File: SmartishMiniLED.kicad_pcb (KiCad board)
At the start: 2 copper layers, 24.9 x 55.4 mm, 35 parts, among them J1 USB_C_Receptacle_USB2.0, J2 BUTTON, J3 Screw_Terminal_01x03, P1 NeopixelStripPads, P2 NeopixelStripPads, Q1 MMBT2222, Q2 MMBT2222, Q3 IRLML6344, Q4 IRF7410, SW2 TL3342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

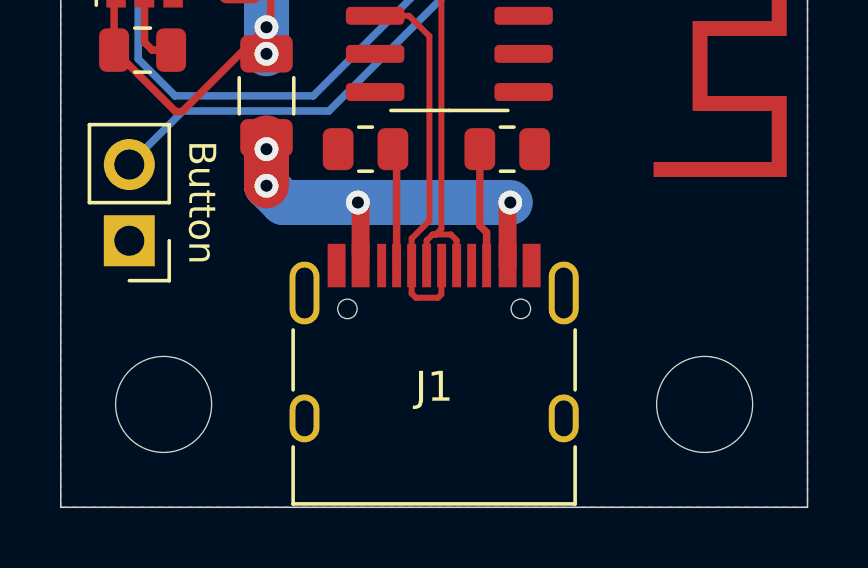
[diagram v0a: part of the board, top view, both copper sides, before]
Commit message: Added some pads on the back for as an alternative to supplying the main power.
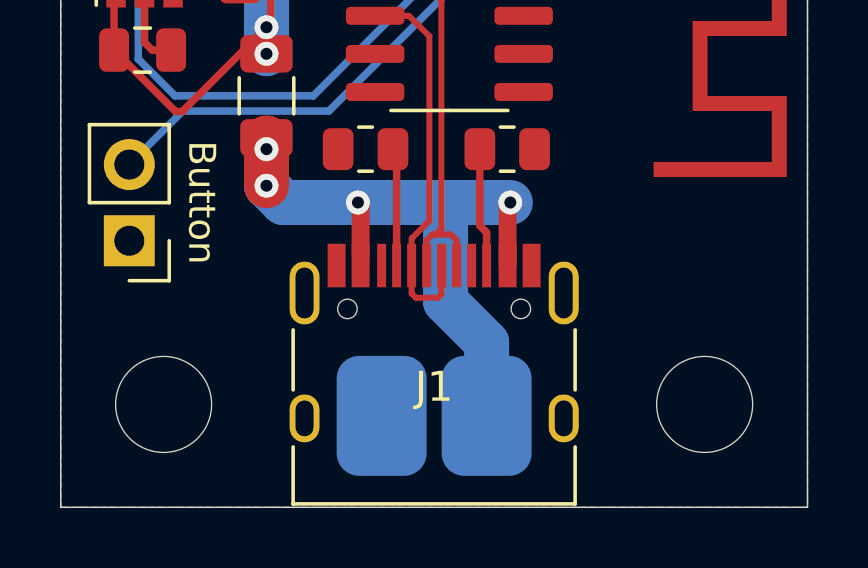
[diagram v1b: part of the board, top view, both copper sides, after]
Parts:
- added J4: Conn_01x02, SmartishMiniLED:Main_Power, B.Cu at (149.4, 112.8)
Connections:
- net Net-(F1-Pad1) renamed /+5V_In
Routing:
- net /+5V_In: track 15.4 -> 23.1 mm
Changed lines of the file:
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@@
     )
   )
-  (property "date" "2022-08-02")
-  (property "version" "d02d224")
+  (property "date" "2022-08-03")
+  (property "version" "bd43bc3")
   (net 0 "")
   (net 1 "VBUS")
@@
   (net 5 "+5V")
   (net 6 "Net-(AE1-Pad2)")
-  (net 7 "Net-(F1-Pad1)")
+  (net 7 "/+5V_In")
   (net 8 "/D-")
   (net 9 "/D+")
@@
       (net 67 "GND") (pinfunction "GND") (pintype "passive"))
     (pad "A4" smd rect locked (at -2.45 -4.045) (size 0.6 1.45) (layers "F.Cu" "F.Paste" "F.Mask")
-      (net 7 "Net-(F1-Pad1)") (pinfunction "VBUS") (pintype "passive"))
+      (net 7 "/+5V_In") (pinfunction "VBUS") (pintype "passive"))
     (pad "A5" smd rect locked (at -1.25 -4.045) (size 0.3 1.45) (layers "F.Cu" "F.Paste" "F.Mask")
       (net 18 "Net-(J1-PadA5)") (pinfunction "CC1") (pintype "bidirectional"))
@@
       (net 22 "unconnected-(J1-PadA8)") (pinfunction "SBU1") (pintype "bidirectional+no_connect"))
     (pad "A9" smd rect locked (at 2.45 -4.045) (size 0.6 1.45) (layers "F.Cu" "F.Paste" "F.Mask")
-      (net 7 "Net-(F1-Pad1)") (pinfunction "VBUS") (pintype "passive"))
+      (net 7 "/+5V_In") (pinfunction "VBUS") (pintype "passive"))
     (pad "A12" smd rect locked (at 3.25 -4.045) (size 0.6 1.45) (layers "F.Cu" "F.Paste" "F.Mask")
       (net 67 "GND") (pinfunction "GND") (pintype "passive"))
@@
       (net 67 "GND") (pinfunction "GND") (pintype "passive"))
     (pad "B4" smd rect locked (at 2.45 -4.045) (size 0.6 1.45) (layers "F.Cu" "F.Paste" "F.Mask")
-      (net 7 "Net-(F1-Pad1)") (pinfunction "VBUS") (pintype "passive"))
+      (net 7 "/+5V_In") (pinfunction "VBUS") (pintype "passive"))
     (pad "B5" smd rect locked (at 1.75 -4.045) (size 0.3 1.45) (layers "F.Cu" "F.Paste" "F.Mask")
       (net 19 "Net-(J1-PadB5)") (pinfunction "CC2") (pintype "bidirectional"))
@@
       (net 15 "unconnected-(J1-PadB8)") (pinfunction "SBU2") (pintype "bidirectional+no_connect"))
     (pad "B9" smd rect locked (at -2.45 -4.045) (size 0.6 1.45) (layers "F.Cu" "F.Paste" "F.Mask")
-      (net 7 "Net-(F1-Pad1)") (pinfunction "VBUS") (pintype "passive"))
+      (net 7 "/+5V_In") (pinfunction "VBUS") (pintype "passive"))
     (pad "B12" smd rect locked (at -3.25 -4.045) (size 0.6 1.45) (layers "F.Cu" "F.Paste" "F.Mask")
       (net 67 "GND") (pinfunction "GND") (pintype "passive"))
@@
     (fp_line (start 1.6 -0.8) (end 1.6 0.8) (layer "F.Fab") (width 0.1))
     (pad "1" smd roundrect (at -1.4 0 90) (size 1.25 1.75) (layers "F.Cu" "F.Paste" "F.Mask") (roundrect_rratio 0.2)
-      (net 7 "Net-(F1-Pad1)") (pintype "passive"))
+      (net 7 "/+5V_In") (pintype "passive"))
     (pad "2" smd roundrect (at 1.4 0 90) (size 1.25 1.75) (layers "F.Cu" "F.Paste" "F.Mask") (roundrect_rratio 0.2)
       (net 5 "+5V") (pintype "passive"))
@@
       (rotate (xyz 0 0 0))
     )
+  )
+  (footprint "SmartishMiniLED:Main_Power" (layer "B.Cu")
+    (at 149.352 112.776 180)
+    (property "Sheetfile" "SmartishMiniLED.kicad_sch")
+    (property "Sheetname" "")
+    (attr smd)
+    (fp_text reference "J4" (at 0 3.81 unlocked) (layer "B.SilkS")
+      (effects (font (size 1 1) (thickness 0.15)) (justify mirror))
+    )
+    (fp_text value "Conn_01x02" (at 0 -3.81 unlocked) (layer "B.Fab")
+      (effects (font (size 1 1) (thickness 0.15)) (justify mirror))
+    )
+    (pad "1" smd roundrect (at -1.75 0 90) (size 4 3) (layers "B.Cu" "B.Paste" "B.Mask") (roundrect_rratio 0.25)
+      (net 7 "/+5V_In") (pinfunction "Pin_1") (pintype "passive"))
+    (pad "2" smd roundrect (at 1.75 0 90) (size 4 3) (layers "B.Cu" "B.Paste" "B.Mask") (roundrect_rratio 0.25)
+      (net 67 "GND") (pinfunction "Pin_2") (pintype "passive"))
   )
   (footprint "SmartishMiniLED:LedStripPads" (layer "B.Cu")
@@
   (via (at 151.892 105.664) (size 0.8) (drill 0.4) (layers "F.Cu" "B.Cu") (net 7))
   (via (at 143.764 105.1052) (size 0.8) (drill 0.4) (layers "F.Cu" "B.Cu") (net 7))
-  (segment (start 151.892 105.664) (end 146.812 105.664) (width 1.5) (layer "B.Cu") (net 7))
   (segment (start 143.764 105.1052) (end 143.764 103.886) (width 1.5) (layer "B.Cu") (net 7))
+  (segment (start 151.102 110.335) (end 149.733 108.966) (width 1.5) (layer "B.Cu") (net 7))
+  (segment (start 149.733 105.664) (end 146.812 105.664) (width 1.5) (layer "B.Cu") (net 7))
   (segment (start 143.764 105.1052) (end 144.3228 105.664) (width 1.5) (layer "B.Cu") (net 7))
   (segment (start 144.3228 105.664) (end 146.812 105.664) (width 1.5) (layer "B.Cu") (net 7))
+  (segment (start 149.733 108.966) (end 149.733 105.664) (width 1.5) (layer "B.Cu") (net 7))
+  (segment (start 151.892 105.664) (end 149.733 105.664) (width 1.5) (layer "B.Cu") (net 7))
+  (segment (start 151.102 112.776) (end 151.102 110.335) (width 1.5) (layer "B.Cu") (net 7))
   (segment (start 148.602 106.864994) (end 149.19448 106.272514) (width 0.2) (layer "F.Cu") (net 8))
   (segment (start 148.602 106.864994) (end 148.602 107.7658) (width 0.2) (layer "F.Cu") (net 8))

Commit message: Updates for production
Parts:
- R7: footprint Resistor_SMD:R_0805_2012Metric_Pad1.20x1.40mm_HandSolder -> Resistor_SMD:R_0805_2012Metric
- R8, R9: value 10k -> 10K; footprint Resistor_SMD:R_0805_2012Metric_Pad1.20x1.40mm_HandSolder -> Resistor_SMD:R_0805_2012Metric
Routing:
- net /+5V_In: track 23.1 -> 15.4 mm

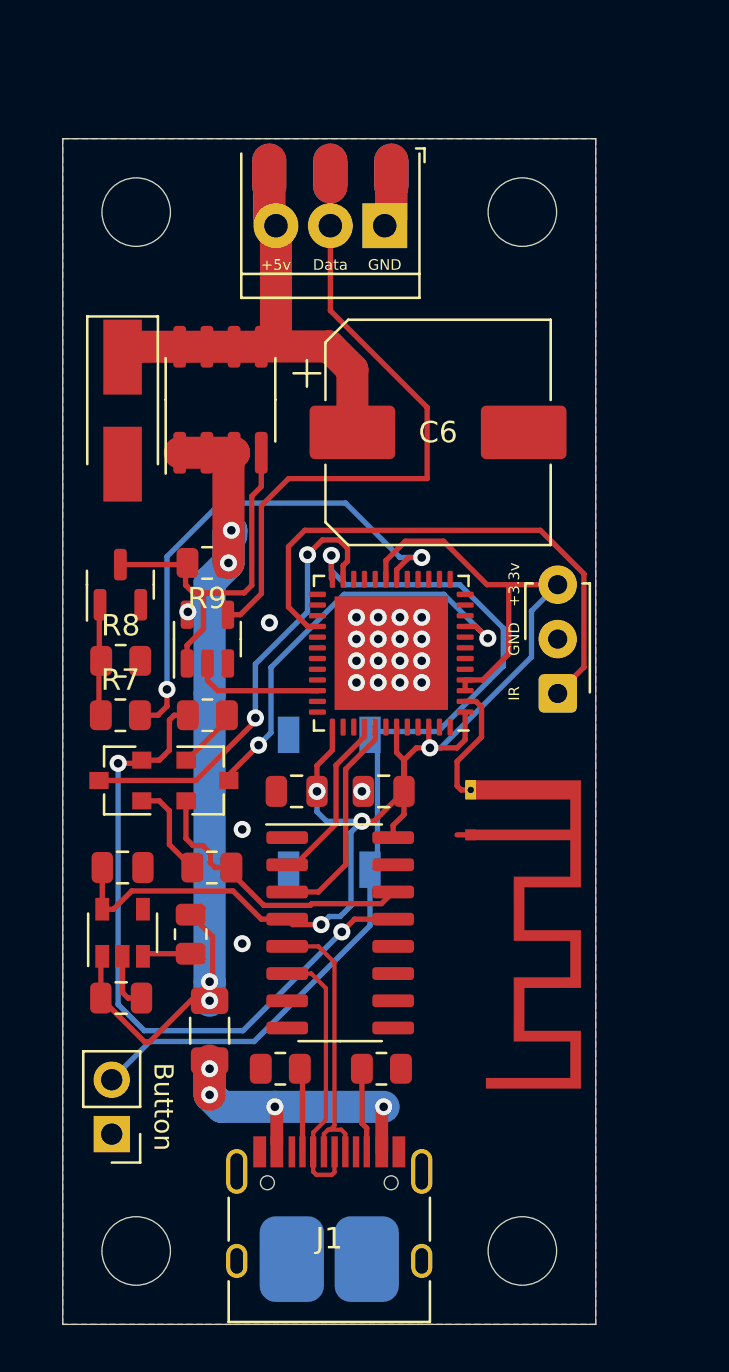
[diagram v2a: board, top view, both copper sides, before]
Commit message: Fixed DRC errors
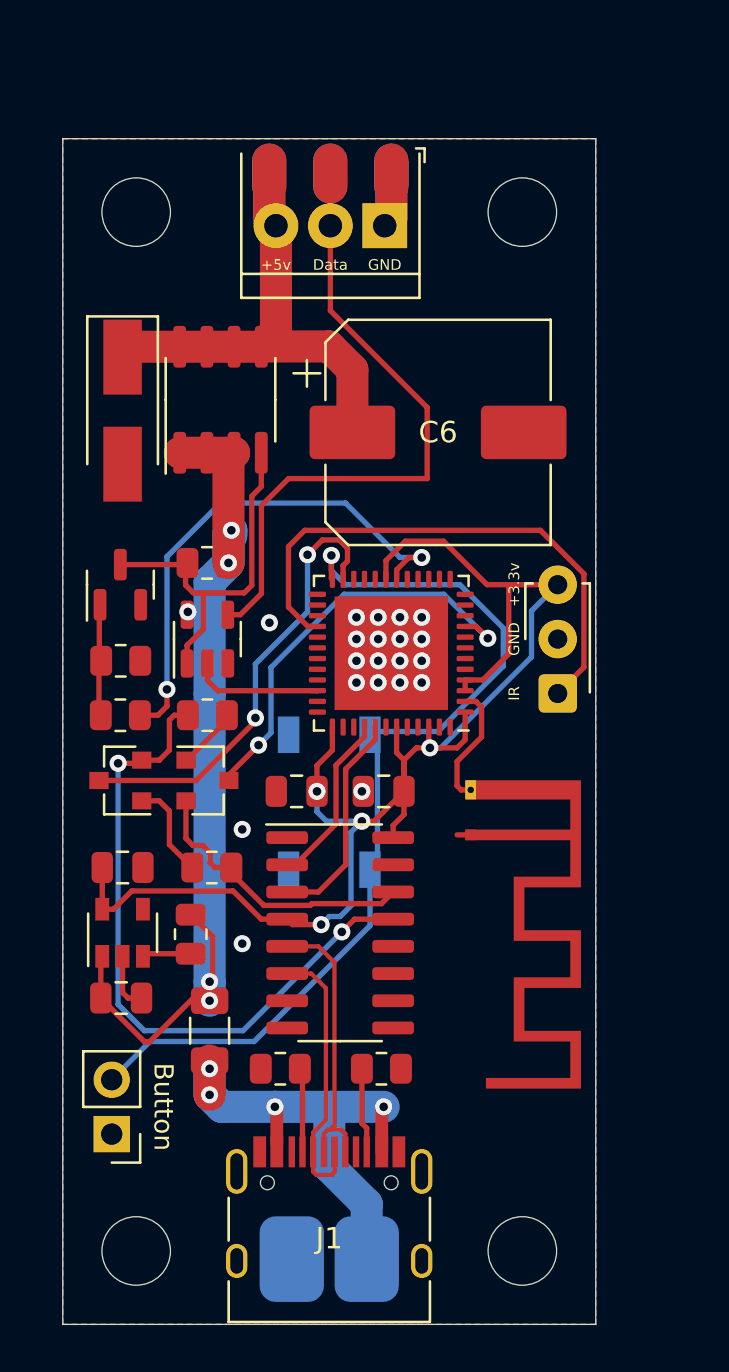
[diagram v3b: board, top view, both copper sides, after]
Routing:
- net /+5V_In: track 15.4 -> 23.3 mm
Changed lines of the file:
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@@
     (property "Sheetname" "")
     (attr smd)
-    (fp_text reference "R9" (at 0 -1.65 180) (layer "F.SilkS")
+    (fp_text reference "R9" (at 0 -0.127 180) (layer "F.SilkS") hide
       (effects (font (size 1 1) (thickness 0.15)))
     )
@@
     (property "Sheetname" "")
     (attr smd)
-    (fp_text reference "R7" (at 0 -1.65) (layer "F.SilkS")
+    (fp_text reference "R7" (at -0.0235 0) (layer "F.SilkS") hide
       (effects (font (size 1 1) (thickness 0.15)))
     )
@@
     (property "Sheetname" "")
     (attr smd)
-    (fp_text reference "R8" (at 0 -1.65) (layer "F.SilkS")
+    (fp_text reference "R8" (at -0.0395 0) (layer "F.SilkS") hide
       (effects (font (size 1 1) (thickness 0.15)))
     )
@@
   (via (at 151.892 105.664) (size 0.8) (drill 0.4) (layers "F.Cu" "B.Cu") (net 7))
   (via (at 143.764 105.1052) (size 0.8) (drill 0.4) (layers "F.Cu" "B.Cu") (net 7))
-  (segment (start 151.892 105.664) (end 146.812 105.664) (width 1.5) (layer "B.Cu") (net 7))
+  (segment (start 151.892 105.664) (end 149.479 105.664) (width 1.5) (layer "B.Cu") (net 7))
+  (segment (start 149.352 105.791) (end 149.479 105.664) (width 1.5) (layer "B.Cu") (net 7))
   (segment (start 143.764 105.1052) (end 143.764 103.886) (width 1.5) (layer "B.Cu") (net 7))
+  (segment (start 149.352 108.458) (end 149.352 105.791) (width 1.5) (layer "B.Cu") (net 7))
+  (segment (start 151.102 112.776) (end 151.102 110.208) (width 1.5) (layer "B.Cu") (net 7))
   (segment (start 143.764 105.1052) (end 144.3228 105.664) (width 1.5) (layer "B.Cu") (net 7))
+  (segment (start 149.479 105.664) (end 146.812 105.664) (width 1.5) (layer "B.Cu") (net 7))
   (segment (start 144.3228 105.664) (end 146.812 105.664) (width 1.5) (layer "B.Cu") (net 7))
+  (segment (start 151.102 110.208) (end 149.352 108.458) (width 1.5) (layer "B.Cu") (net 7))
   (segment (start 148.602 106.864994) (end 149.19448 106.272514) (width 0.2) (layer "F.Cu") (net 8))
   (segment (start 148.602 106.864994) (end 148.602 107.7658) (width 0.2) (layer "F.Cu") (net 8))

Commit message: Reworked using the WROOM-32D module
This allows for easier manufacrure
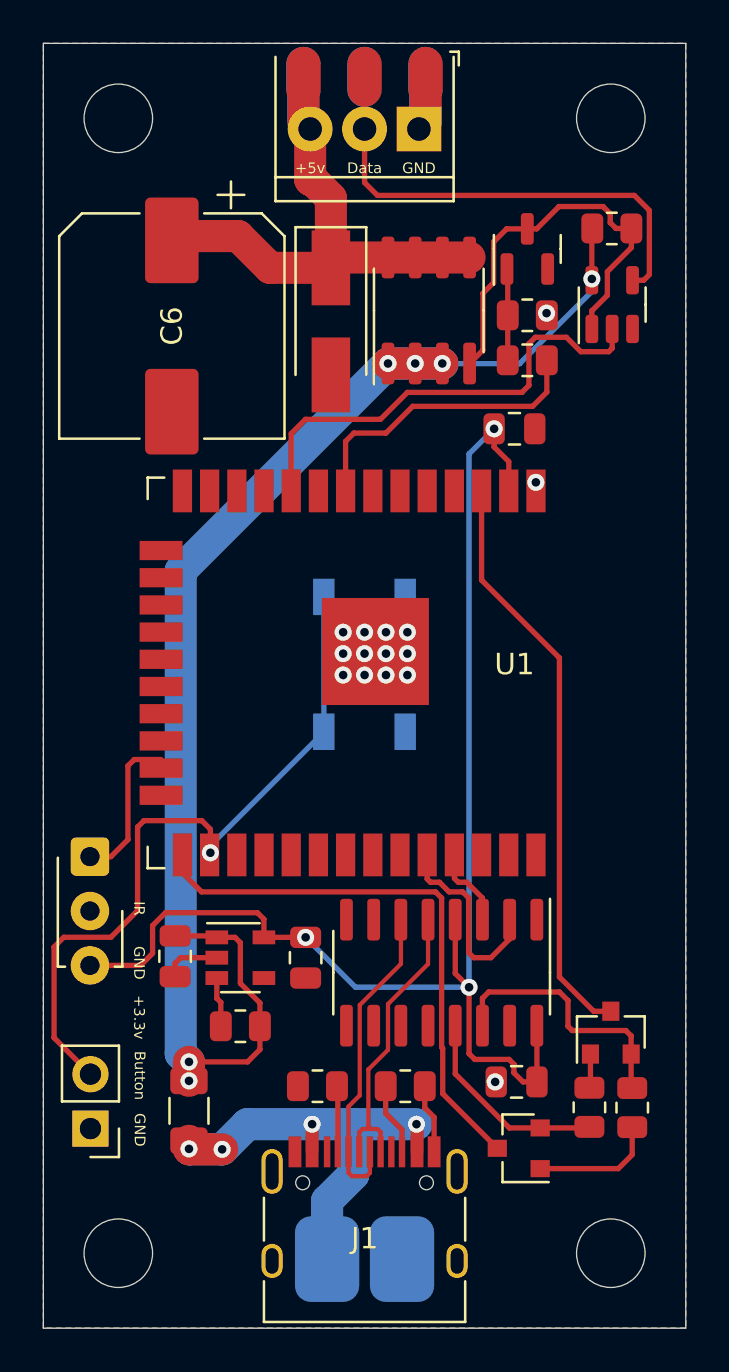
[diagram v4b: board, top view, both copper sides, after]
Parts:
- removed AE1: Antenna_Chip, SmartishMiniLED:Texas_SWRA117D_2.4GHz_Right
- U1: value ESP32-PICO-D4 -> ESP32-WROOM-32D; footprint Package_DFN_QFN:QFN-48-1EP_7x7mm_P0.5mm_EP5.3x5.3mm -> RF_Module:ESP32-WROOM-32
- moved R3 25.6 mm to (161.5, 105.7), turned to -90 degrees
- moved Q1 25.3 mm to (158.2, 107.6)
- moved R7 25.2 mm to (158.6, 70.8)
- moved R8 24.9 mm to (158.6, 68.7)
- moved Q3 24.6 mm to (158.6, 65.6)
- moved R9 24.5 mm to (162.5, 64.6), turned to 0 degrees
- moved U4 24.5 mm to (162.6, 68.2)
- moved U5 23.1 mm to (138.2, 94.0), turned to -90 degrees
- moved R2 22.6 mm to (163.5, 105.7), turned to 90 degrees
- moved Q2 22.2 mm to (162.5, 102.2), turned to 90 degrees
- moved C5 18.0 mm to (158.0, 74.0), turned to 0 degrees
- moved C3 17.0 mm to (158.1, 104.5)
- moved C6 13.4 mm to (142.0, 69.2), turned to -90 degrees
- moved Q4 10.6 mm to (154.0, 68.5)
- moved D1 10.6 mm to (149.4, 69.0)
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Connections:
- U1 pad 1: +3V3 -> GND
- U1 pad 10: unconnected-(U1-Pad10) -> /NEOPIXEL
- U1 pad 15: unconnected-(U1-Pad15) -> GND
- U1 pad 18: /LED_POWER -> unconnected-(U1-Pad18)
- U1 pad 19: +3V3 -> unconnected-(U1-Pad19)
- U1 pad 2: Net-(AE1-Pad2) -> +3V3
- U1 pad 23: /GPIO0 -> /IR
- U1 pad 24: /BUTTON -> unconnected-(U1-Pad24)
- U1 pad 25: unconnected-(U1-Pad25) -> /GPIO0
- U1 pad 26: unconnected-(U1-Pad26) -> /BUTTON
- U1 pad 28: /IR -> unconnected-(U1-Pad28)
- U1 pad 3: +3V3 -> /RESET
- U1 pad 34: /NEOPIXEL -> /RXD0
- U1 pad 35: unconnected-(U1-Pad35) -> /TXD0
- U1 pad 37: +3V3 -> unconnected-(U1-Pad37)
- U1 pad 38: unconnected-(U1-Pad38) -> GND
- U1 pad 39: unconnected-(U1-Pad39) -> GND
- U1 pad 4: +3V3 -> unconnected-(U1-Pad4)
- U1 pad 8: unconnected-(U1-Pad8) -> /LED_POWER
- U1 pad 9: /RESET -> unconnected-(U1-Pad9)
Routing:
- net /DTR: track 31.8 -> 9.51 mm, vias 2 -> 0
- net +5V: track 44.5 -> 66.2 mm, vias 5 -> 6
- net /IR: track 25.6 -> 7.22 mm
- net /NEOPIXEL: track 6.13 -> 21.5 mm
- net /BUTTON: track 44.6 -> 34.1 mm
- net /LED_POWER: track 24.2 -> 13.8 mm, vias 2 -> 0
- net /RESET: track 19.8 -> 27.7 mm, vias 2 -> 0
- net /DATA_OUT: track 32.9 -> 25.1 mm
- net /TXD0: track 10.3 -> 4.20 mm
- net Net-(AE1-Pad2): track 5.74 -> 0.00 mm
- net /GPIO0: track 21.1 -> 26.6 mm, vias 2 -> 0
- net +3V3: track 67.4 -> 63.9 mm, vias 4 -> 3
- net /D-: track 13.0 -> 14.9 mm
- net /DATA_ENABLE: track 17.5 -> 19.4 mm
- net /RXD0: track 8.15 -> 9.66 mm
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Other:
- board size 24.9 x 55.4 mm -> 30 x 60 mm

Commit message: Fixed 3D models
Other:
- board text added: "5V"
